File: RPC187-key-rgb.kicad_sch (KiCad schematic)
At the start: 87 parts

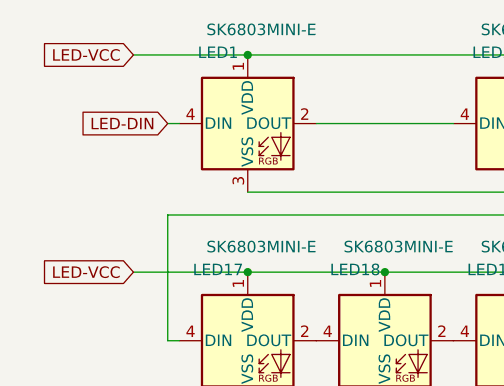
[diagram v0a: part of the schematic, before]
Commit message: Wider LED VCC traces
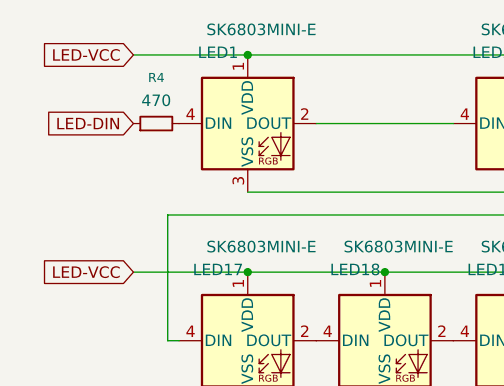
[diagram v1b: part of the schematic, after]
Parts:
- added R4: 470, ScottoKeebs_Components:Resistor_0402, symbol Device:R_Small
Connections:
- net LED-DIN: now also R4.1; no longer LED1.4 (DIN)
- new net: LED1.4 (DIN), R4.2
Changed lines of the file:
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@@
-	(wire
-		(pts
-			(xy 30.48 45.72) (xy 31.75 45.72)
-		)
-		(stroke
-			(width 0)
-			(type default)
-		)
-	)
 	(wire
 		(pts
@@
 	(global_label "LED-DIN"
 		(shape input)
-		(at 30.48 45.72 180)
+		(at 26.67 45.72 180)
 		(fields_autoplaced yes)
 		(effects
@@
 		)
 		(property "Intersheetrefs" "${INTERSHEET_REFS}"
-			(at 19.27 45.72 0)
+			(at 15.46 45.72 0)
 			(effects
 				(font
@@
 					(unit 1)
 				)
+			)
+		)
+	)
+	(symbol
+		(lib_id "Device:R_Small")
+		(at 29.21 45.72 90)
+		(unit 1)
+		(exclude_from_sim no)
+		(in_bom yes)
+		(on_board yes)
+		(dnp no)
+		(property "Reference" "R4"
+			(at 29.21 40.64 90)
+			(effects
+				(font
+					(size 1.016 1.016)
+				)
+			)
+		)
+		(property "Value" "470"
+			(at 29.21 43.18 90)
+			(effects
+				(font
+					(size 1.27 1.27)
+				)
+			)
+		)
+		(property "Footprint" "ScottoKeebs_Components:Resistor_0402"
+			(at 29.21 45.72 0)
+			(effects
+				(font
+					(size 1.27 1.27)
+				)
+				(hide yes)
+			)
+		)
+		(property "Datasheet" "~"
+			(at 29.21 45.72 0)
+			(effects
+				(font
+					(size 1.27 1.27)
+				)
+				(hide yes)
+			)
+		)
+		(property "Description" "Resistor, small symbol"
+			(at 29.21 45.72 0)
+			(effects
+				(font
+					(size 1.27 1.27)
+				)
+				(hide yes)
+			)
+		)
+		(pin "2"
+		)
+		(pin "1"
+		)
+		(instances
+			(project ""
+				(path "/95a398a3-530a-498f-83e6-54659633b68d/2e208cc2-66a7-45cf-b7d2-709f4d024098"
+					(reference "R4")
+					(unit 1)
+				)
